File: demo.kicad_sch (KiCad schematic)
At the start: 32 parts, among them J2 Conn_01x06, J3 Conn_01x04, J4 USB_C_Receptacle, U1 Regulator_Linear_XC6220B331MR, U2 MCU_ST_STM32F1_STM32F103C8Tx, Y2 8M

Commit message: update sch
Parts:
- removed C2, C7: 10uF, Capacitor_SMD:C_0603_1608Metric, symbol demo-rescue:CP-Device
- removed J2: Conn_01x06, Connector_PinHeader_1.27mm:PinHeader_1x06_P1.27mm_Horizontal, symbol Connector_Generic:Conn_01x06
- removed J4: USB_C_Receptacle, selfdefined_library:USB_C_Receptacle_24Pin_Hole_SMD, symbol Connector:USB_C_Receptacle
- removed R6, R7: 22, Resistor_SMD:R_0402_1005Metric, symbol Device:R
- removed U1: Regulator_Linear_XC6220B331MR, Package_TO_SOT_SMD:SOT-23-5, symbol demo-rescue:XC6220B331MR-Regulator_Linear
- added C2: 10uF, Capacitor_SMD:C_0603_1608Metric, symbol Device:C
- added C7: 10UF, Capacitor_SMD:C_0603_1608Metric, symbol Device:C
- added D3: BAT60JFILM, Diode_SMD:D_SOD-323, symbol Diode:BAT60A
- added J1: Conn_02x05_Odd_Even, Connector_PinHeader_2.54mm:PinHeader_2x05_P2.54mm_Horizontal, symbol Connector_Generic:Conn_02x05_Odd_Even
- added J2: USB_C_Receptacle, Connector_USB:USB_C_Receptacle_Amphenol_12401610E4-2A, symbol Connector:USB_C_Receptacle
- added JP1: Jumper_2_Bridged, Connector_PinHeader_2.54mm:PinHeader_1x02_P2.54mm_Vertical, symbol Jumper:Jumper_2_Bridged
- added Q1: S9013, Package_TO_SOT_SMD:SOT-23, symbol Transistor_BJT:Q_NPN_BEC
- added R14, R17, R18: 10K, Resistor_SMD:R_0402_1005Metric, symbol Device:R
- added R15: 36K, Resistor_SMD:R_0402_1005Metric, symbol Device:R
- added R16: 100R, Resistor_SMD:R_0402_1005Metric, symbol Device:R
- added R19, R20, R21, R22, R23: 22, Resistor_SMD:R_0402_1005Metric, symbol Device:R
- added R24: 100, Resistor_SMD:R_0402_1005Metric, symbol Device:R
- added U1: AMS1117-3.3, Package_TO_SOT_SMD:SOT-223-3_TabPin2, symbol Regulator_Linear:AMS1117-3.3
- R4, R5: value 22 -> 10
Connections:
- net +3V3: now also C2.1, J1.1 (Pin_1), JP1.1 (A), Q1.3 (C), U1.2 (VO); no longer R8.1
- net +5V: now also C7.1, J1.2 (Pin_2), J2.A4 (VBUS), J2.A9 (VBUS), J2.B4 (VBUS), J2.B9 (VBUS), R14.1, U1.3 (VI)
- net BOOT0: now also R9.2; no longer R9.1
- net GND: now also R9.1, C2.2, C7.2, J1.4 (Pin_4), J2.A1 (GND), J2.A12 (GND), J2.B1 (GND), J2.B12 (GND), J2.S1 (SHIELD), R15.2, R17.1, R18.1, R23.1, U1.1 (GND); no longer R9.2
- net SWCLK: now also J1.6 (Pin_6), R19.2; no longer R4.2
- net SWDIO: now also J1.5 (Pin_5), R20.1; no longer R5.2
- net T_JTCK: now also R19.1; no longer R4.1
- net T_JTMS: now also R20.2; no longer R5.1
- net T_NRST: now also R21.2
- net AIN: now reaches R12.1, R13.2, U2.10 (PA0)
- net AIN: now also R24.1
- net T_Tx: now reaches U2.12 (PA2)
- net T_Tx: now also J1.9 (Pin_9)
- net T_Rx: now reaches U2.13 (PA3)
- net T_Rx: now also J1.10 (Pin_10)
- net at U2.2 (PC13): now also R17.2
- net at U2.3 (PC14): now also R18.2
- net RENUM: now reaches U2.38 (PA15)
- net RENUM: now also R16.2
- net at R3.2: now also J2.A5 (CC1), J2.B5 (CC2)
- net STLINK_USB_DM- renamed DM-
- net DM-: now also R5.1
- net STLINK_USB_DP+: no longer names the net of R8.2
- net STLINK_USB_DP+: now also R4.2, J2.A6 (D+), J2.B6 (D+); no longer U2.33 (PA12)
- net SWO renamed T_SWO
- net T_SWO: now also R22.1
- net T_SWDIO_IN: no longer names the net of R10.1, U2.25 (PB12)
- new net: D3.1 (K), R24.2
- new net: D3.2 (A), J1.3 (Pin_3), JP1.2 (B), R23.2
- new net: Q1.1 (B), R14.2, R15.1, R16.1
- new net: Q1.2 (E), R8.1
- new net: J1.7 (Pin_7), R21.1
- new net: J1.8 (Pin_8), R22.2
- new net: J2.A7 (D-), J2.B7 (D-), R5.2
- new net DP+: R4.1, U2.33 (PA12)
- no-connect marks 32 -> 27
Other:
- moved on the sheet: C10, C11, C9, J3, R10, R11, R12, R13, R8, R9, U2

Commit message: update sch
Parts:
- removed D3: BAT60JFILM, Diode_SMD:D_SOD-323, symbol Diode:BAT60A
- removed JP1: Jumper_2_Bridged, Connector_PinHeader_2.54mm:PinHeader_1x02_P2.54mm_Vertical, symbol Jumper:Jumper_2_Bridged
- removed R23: 22, Resistor_SMD:R_0402_1005Metric, symbol Device:R
- removed R24: 100, Resistor_SMD:R_0402_1005Metric, symbol Device:R
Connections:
- net GND: now also J1.3 (Pin_3)
- net AIN: no longer names the net of R12.1, R13.2, U2.10 (PA0)
- net SWCLK: no longer names the net of J1.6 (Pin_6), R19.2
- net SWDIO: no longer names the net of J1.5 (Pin_5), R20.1
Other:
- moved on the sheet: R19, R20, R21, R22

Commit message: V1.0.2
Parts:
- added R14, R15: 22, Resistor_SMD:R_0402_1005Metric, symbol Device:R
- added R21: 100, Resistor_SMD:R_0402_1005Metric, symbol Device:R
- C1: value 100nF -> 10uF; footprint Capacitor_SMD:C_0402_1005Metric -> Capacitor_SMD:C_0603_1608Metric
- C2: renamed from C7; value 10UF -> 100nF; footprint Capacitor_SMD:C_0603_1608Metric -> Capacitor_SMD:C_0402_1005Metric
- C3: renamed from C2; value 10uF -> 22uF
- D1: value LED -> LED_RED
- D2: value LED -> LED_GREEN
- J1: renamed from J2; footprint Connector_USB:USB_C_Receptacle_Amphenol_12401610E4-2A -> Library:USB_C_Receptacle_typecf 双排 SMT六孔
- R7: renamed from R16; value 100R -> 100
- U2: value MCU_ST_STM32F1_STM32F103C8Tx -> STM32F103C8Tx
- renumbered C9 to C11, C8 to C4, C3 to C5, C4 to C6, C5 to C7, C6 to C8, C11 to C9, J1 to J2, R3 to R1, R20 to R10, R21 to R11, R19 to R12, R22 to R13, R11 to R16, R9 to R17, R10 to R18, R17 to R19, R5 to R2, R18 to R20, R12 to R22, R13 to R23, R4 to R3, R8 to R4, R14 to R5, R15 to R6, R1 to R8, R2 to R9, Y2 to Y1
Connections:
- net DP+: now also R4.2
- net GND: now also R21.1; no longer U2.20 (PB2)
- net STM_JTCK: now also R15.1; no longer J3.3 (Pin_3)
- net STM_JTMS: now also R14.1; no longer J3.2 (Pin_2)
- net at J1.A6 (D+), J1.B6 (D+), R3.2: no longer R4.2
- new net: R21.2, U2.20 (PB2)
- new net: J3.2 (Pin_2), R14.2
- new net: J3.3 (Pin_3), R15.2
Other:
- company: DIY -> (none)
- title: STLINK-FAKE -> DIY stlink
- moved on the sheet: C10, C11, C5, C6, C7, C8, D1, D2, J1, J2, J3, Q1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

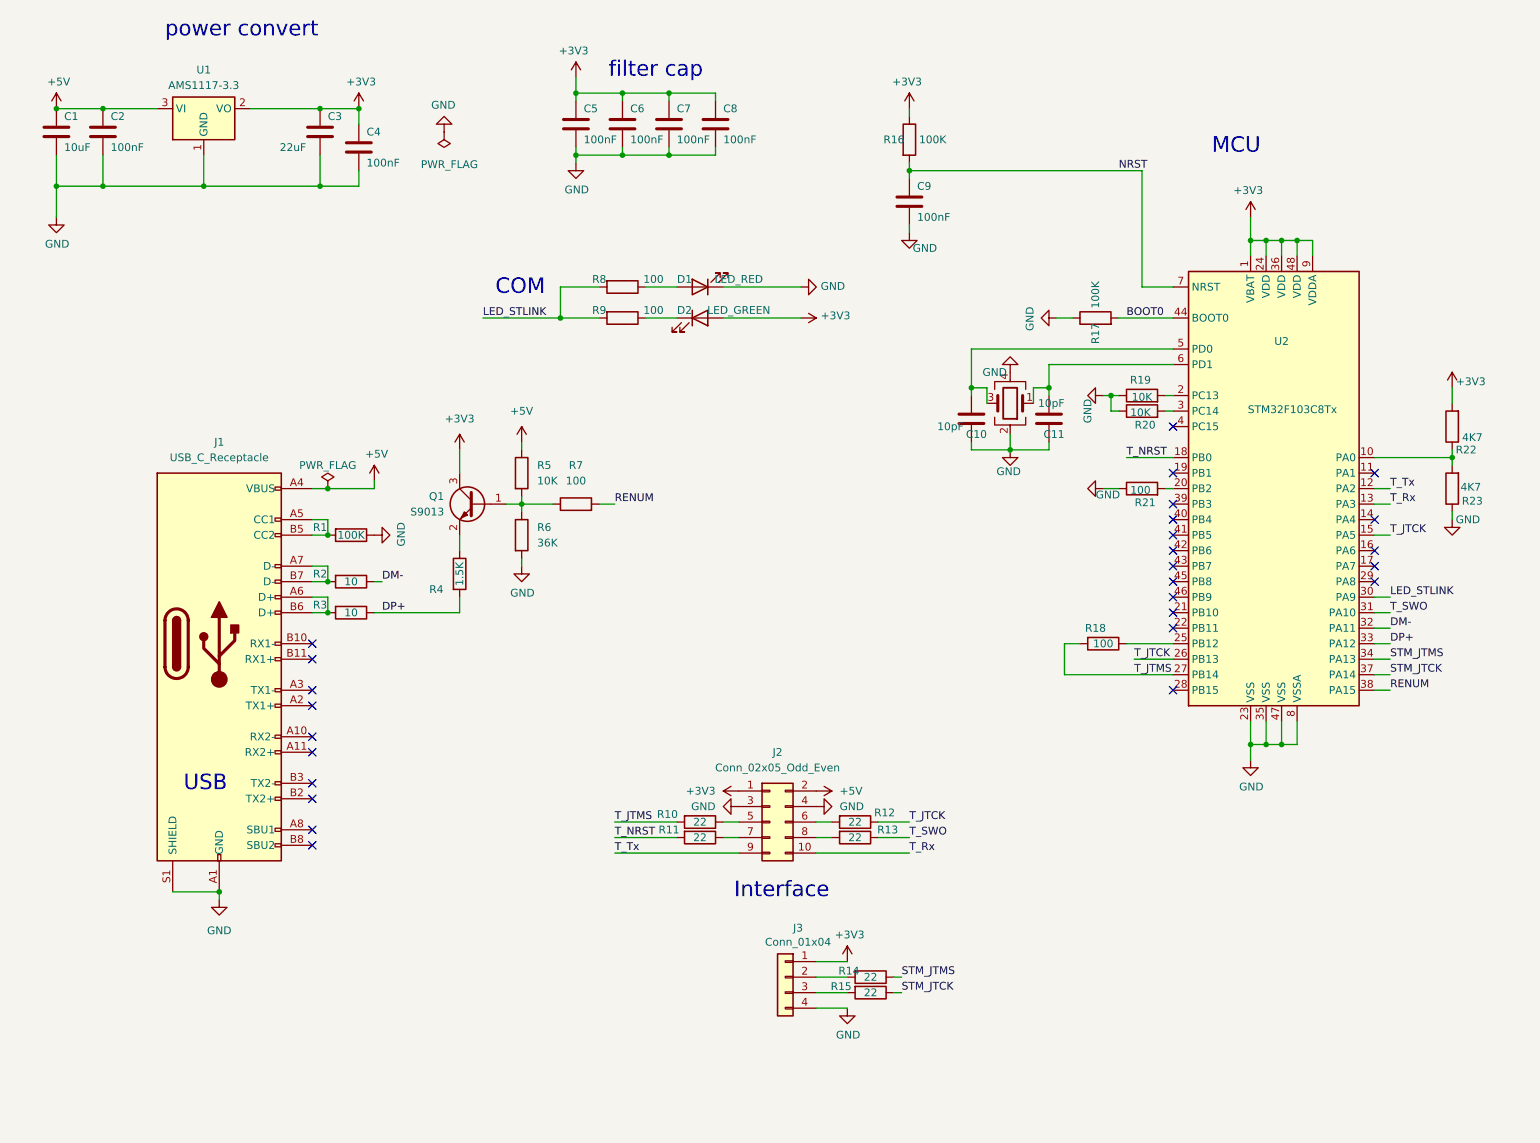
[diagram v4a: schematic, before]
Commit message: 1.3*3.8(cm^2) relayout
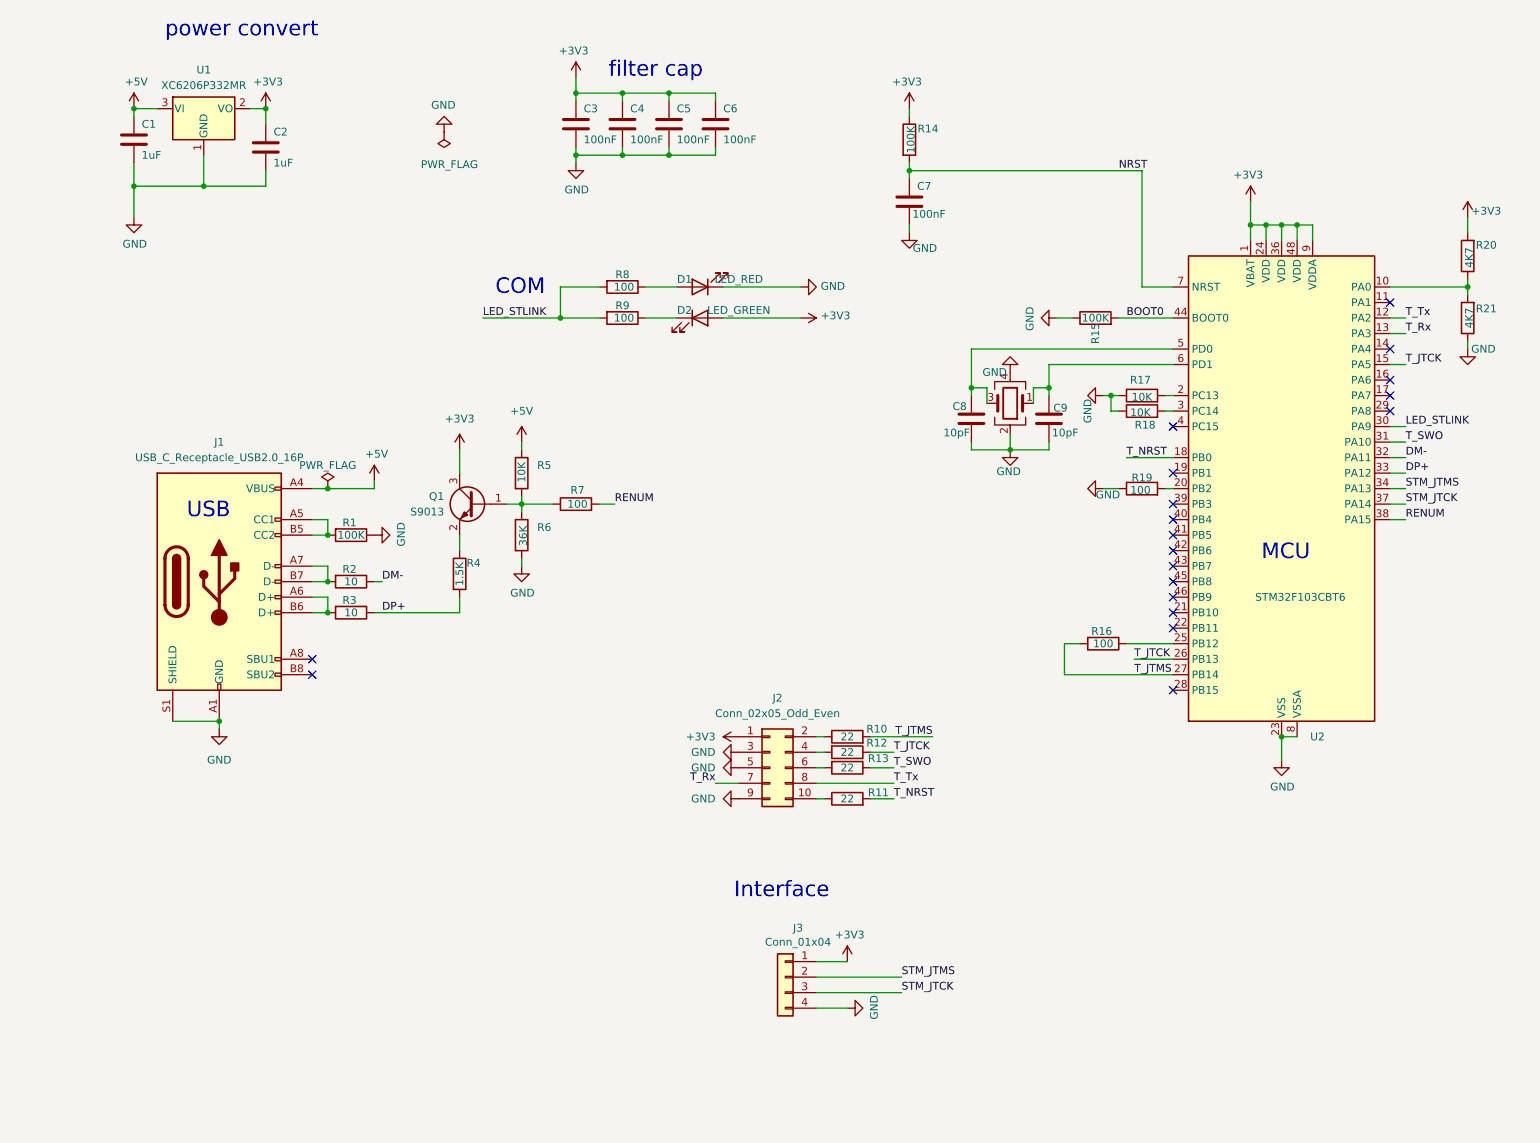
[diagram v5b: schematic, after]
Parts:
- removed C2: 100nF, Capacitor_SMD:C_0402_1005Metric, symbol Device:C
- removed C3: 22uF, Capacitor_SMD:C_0603_1608Metric, symbol Device:C
- removed J1: USB_C_Receptacle, Library:USB_C_Receptacle_typecf 双排 SMT六孔, symbol Connector:USB_C_Receptacle
- removed R14, R15: 22, Resistor_SMD:R_0402_1005Metric, symbol Device:R
- removed U1: AMS1117-3.3, Package_TO_SOT_SMD:SOT-223-3_TabPin2, symbol Regulator_Linear:AMS1117-3.3
- removed U2: STM32F103C8Tx, Package_QFP:LQFP-48_7x7mm_P0.5mm, symbol demo-rescue:STM32F103C8Tx-MCU_ST_STM32F1
- added J1: USB_C_Receptacle_USB2.0_16P, Connector_USB:USB_C_Receptacle_GCT_USB4105-xx-A_16P_TopMnt_Horizontal, symbol Connector:USB_C_Receptacle_USB2.0_16P
- added U1: XC6206P332MR, Package_TO_SOT_SMD:SOT-23-3, symbol Regulator_Linear:XC6206PxxxMR
- added U2: STM32F103CBT6, Package_QFP:LQFP-48_7x7mm_P0.5mm, symbol MCU_ST_STM32F1:STM32F103CBTx
- C1: value 10uF -> 1uF; footprint Capacitor_SMD:C_0603_1608Metric -> Capacitor_SMD:C_0402_1005Metric
- C2: renamed from C4; value 100nF -> 1uF
- renumbered C5 to C3, C6 to C4, C7 to C5, C8 to C6, C9 to C7, C10 to C8, C11 to C9, R16 to R14, R17 to R15, R18 to R16, R19 to R17, R20 to R18, R21 to R19, R22 to R20, R23 to R21
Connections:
- net +3V3: now also U1.2 (VO), U2.1 (VBAT), U2.24 (VDD), U2.36 (VDD), U2.48 (VDD), U2.9 (VDDA)
- net +5V: now also J1.A4 (VBUS), J1.A9 (VBUS), J1.B4 (VBUS), J1.B9 (VBUS), U1.3 (VI); no longer J2.2 (Pin_2)
- net BOOT0: now also U2.44 (BOOT0)
- net DM-: now also U2.32 (PA11)
- net DP+: now also U2.33 (PA12)
- net GND: now also J2.5 (Pin_5), J2.9 (Pin_9), J1.A1 (GND), J1.A12 (GND), J1.B1 (GND), J1.B12 (GND), J1.S1 (SHIELD), U1.1 (GND), U2.23 (VSS), U2.35 (VSS), U2.47 (VSS), U2.8 (VSSA); no longer J2.4 (Pin_4)
- net LED_STLINK: now also U2.30 (PA9)
- net NRST: now also U2.7 (NRST)
- net RENUM: now also U2.38 (PA15)
- net STM_JTCK: now also J3.3 (Pin_3), U2.37 (PA14)
- net STM_JTMS: now also J3.2 (Pin_2), U2.34 (PA13)
- net T_JTCK: now also U2.15 (PA5), U2.26 (PB13)
- net T_JTMS: now also U2.27 (PB14)
- net T_NRST: now also U2.18 (PB0)
- net T_Rx: now also J2.7 (Pin_7), U2.13 (PA3); no longer J2.10 (Pin_10)
- net T_SWO: now also U2.31 (PA10)
- net T_Tx: now also J2.8 (Pin_8), U2.12 (PA2); no longer J2.9 (Pin_9)
- net at R20.1, R21.2: now also U2.10 (PA0)
- net at R17.2: now also U2.2 (PC13)
- net at R19.2: now also U2.20 (PB2)
- net at R16.1: now also U2.25 (PB12)
- net at R18.2: now also U2.3 (PC14)
- net at C8.2, Y1.3: now also U2.5 (PD0)
- net at C9.2, Y1.1: now also U2.6 (PD1)
- net at R10.1: now also J2.2 (Pin_2); no longer J2.5 (Pin_5)
- net at R12.2: now also J2.4 (Pin_4); no longer J2.6 (Pin_6)
- net at R11.1: now also J2.10 (Pin_10); no longer J2.7 (Pin_7)
- net at R13.2: now also J2.6 (Pin_6); no longer J2.8 (Pin_8)
- net at R1.2: now also J1.A5 (CC1), J1.B5 (CC2)
- net at R3.2: now also J1.A6 (D+), J1.B6 (D+)
- net at R2.2: now also J1.A7 (D-), J1.B7 (D-)
- no-connect marks 27 -> 19
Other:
- moved on the sheet: C1, C2, J2, R10, R11, R12, R13, R20, R21

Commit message: V1.0.4
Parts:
- J2: footprint Connector_PinHeader_2.54mm:PinHeader_2x05_P2.54mm_Horizontal -> Library:pin-header-hor-handsolid-2x5
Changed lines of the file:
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@@
 			)
 		)
-		(property "Footprint" "Connector_PinHeader_2.54mm:PinHeader_2x05_P2.54mm_Horizontal"
+		(property "Footprint" "Library:pin-header-hor-handsolid-2x5"
 			(at 140.97 137.16 0)
 			(effects
